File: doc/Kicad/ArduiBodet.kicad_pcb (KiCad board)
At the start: 2 copper layers, 69.8 x 52.6 mm, 22 parts, among them CON1 BARREL_JACK, IC1 ATMEGA328-P, IC2 SN754410, P1 ISP10PIN, P2 DS3231_Breakout_Connector, P3 Moteur Horloge, SW1 SWITCH_INV, SW2 Switch_DPST, U1 LM7805CT

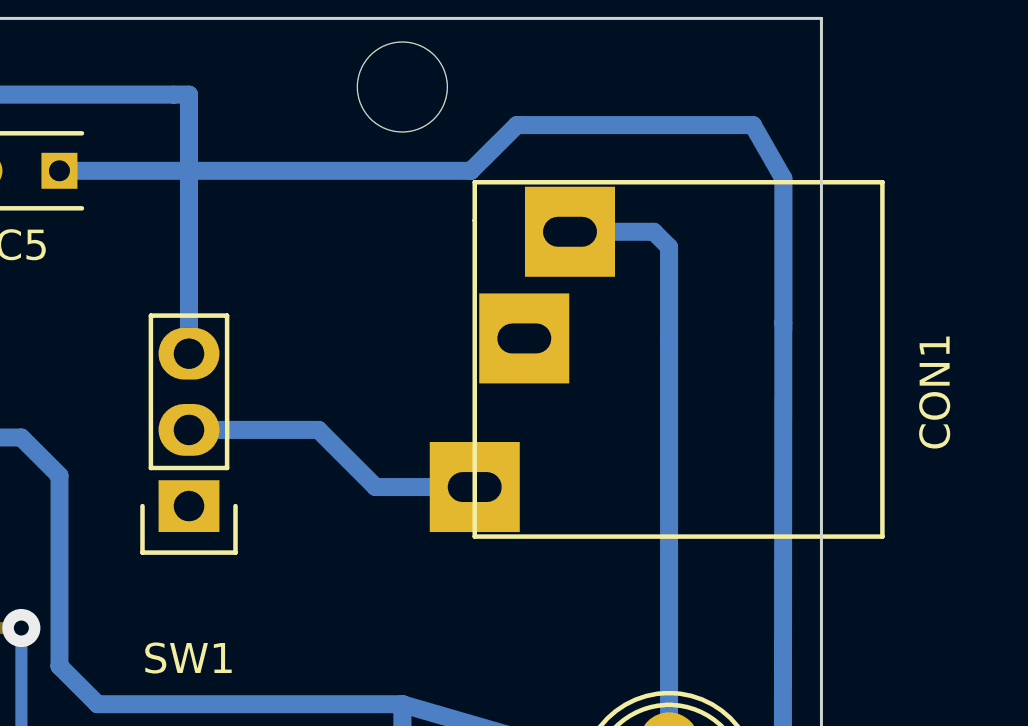
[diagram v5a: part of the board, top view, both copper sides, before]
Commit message: typon terminé et vérifié correction empreinte BARREL_JACK_FR
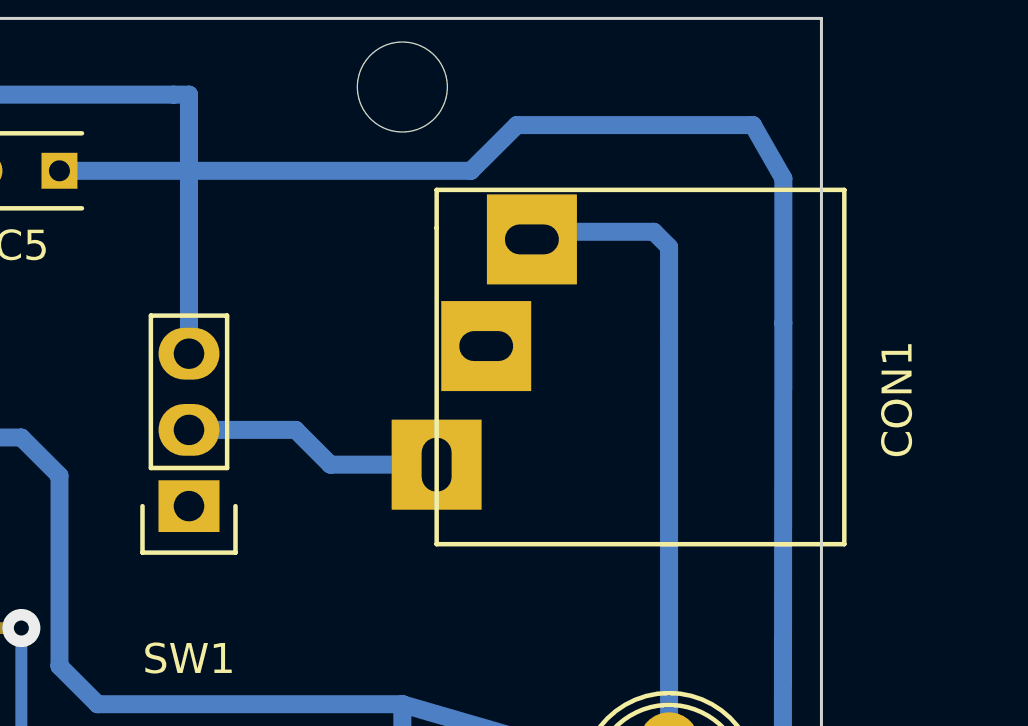
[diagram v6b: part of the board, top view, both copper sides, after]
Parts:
- moved CON1 1.30 mm to (190.5, 99.1)
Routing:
- net Net-(CON1-Pad1): track 10.3 -> 8.74 mm
